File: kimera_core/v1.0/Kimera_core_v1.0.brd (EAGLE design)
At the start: 26 x 12 mm, 15 parts, among them IC1 PCA9555RGER, IC2 PCA9555RGER, Q1 CSTCR6M00G53Z, U1 ATMEGA32U4QFN

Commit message: kimera_core: Change bus and layout
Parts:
- added JP1, JP2, JP3, JP4: (no value), castellation:P12
- moved IC2 18.1 mm to (4.50, 10.5)
- moved C5 10.9 mm to (9.25, 10.0), turned to 90 degrees
- moved C1 4.47 mm to (13.4, 12.0)
- moved C2 4.47 mm to (11.0, 12.0)
- moved C3 4.47 mm to (12.2, 12.0)
- moved Q1 4.47 mm to (21.6, 3.80)
- moved R1 4.47 mm to (13.4, 4.00)
- moved R2 4.47 mm to (12.2, 4.00)
- moved R3 4.47 mm to (11.0, 4.00)
- moved R4 4.47 mm to (23.0, 12.0)
- moved R5 4.47 mm to (21.8, 12.0)
- moved R6 4.47 mm to (20.6, 12.0)
- moved U1 4.47 mm to (17.0, 8.00)
- moved C4 2.73 mm to (9.25, 5.00), turned to 270 degrees
- moved IC1 1.58 mm to (4.50, 4.50)
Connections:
- net N$1 renamed RESET
- net N$11 renamed SDA
- removed net N$10: IC1.19, R5.1, U1.18
- new net A1: IC1.23, IC2.23
- new net A2: IC1.24, IC2.24
- new net MISO: U1.11
- new net MOSI: U1.10
- new net P1: IC1.1, JP2.7
- new net P10: IC1.11, JP1.4
- new net P11: IC1.12, JP1.5
- new net P12: IC1.13, JP1.6
- new net P13: IC1.14, JP1.7
- new net P14: IC1.15, JP1.8
- new net P15: IC1.16, JP1.9
- new net P16: IC1.17, JP1.10
- new net P17: IC2.1, JP3.3
- new net P18: IC2.2, JP3.4
- new net P19: IC2.3, JP3.5
- new net P2: IC1.2, JP2.8
- new net P20: IC2.4, JP3.6
- new net P21: IC2.5, JP3.7
- new net P22: IC2.6, JP3.8
- new net P23: IC2.7, JP3.9
- new net P24: IC2.8, JP3.10
- new net P25: IC2.10, JP3.11
- new net P26: IC2.11, JP3.12
- new net P27: IC2.12, JP2.1
- new net P28: IC2.13, JP2.2
- new net P29: IC2.14, JP2.3
- new net P3: IC1.3, JP2.9
- new net P30: IC2.15, JP2.4
- new net P31: IC2.16, JP2.5
- new net P32: IC2.17, JP2.6
- new net P4: IC1.4, JP2.10
- new net P5: IC1.5, JP2.11
- new net P6: IC1.6, JP2.12
- new net P7: IC1.7, JP1.1
- new net P8: IC1.8, JP1.2
- new net P9: IC1.10, JP1.3
- new net RX: U1.20
- new net SCK: U1.9
- new net SCL: IC1.19, IC2.19, R5.1, U1.18
- new net TX: U1.21
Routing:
- net P17: track 0.00 -> 9.95 mm, vias 0 -> 1
- net P16: track 0.00 -> 9.45 mm, vias 0 -> 1
- net P18: track 0.00 -> 8.39 mm, vias 0 -> 1
- net P15: track 0.00 -> 7.89 mm, vias 0 -> 1
- net P19: track 0.00 -> 6.83 mm, vias 0 -> 1
- net P14: track 0.00 -> 6.33 mm, vias 0 -> 1
- net P20: track 0.00 -> 5.33 mm
- net P21: track 0.00 -> 4.68 mm
- net P13: track 0.00 -> 4.68 mm
- net GND: track 0.00 -> 4.15 mm
- net P26: track 0.00 -> 3.53 mm
- net P32: track 0.00 -> 3.53 mm
- net P27: track 0.00 -> 3.47 mm
- net P12: track 0.00 -> 3.47 mm
- net P22: track 0.00 -> 3.45 mm
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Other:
- board size 26 x 12 mm -> 25 x 15 mm

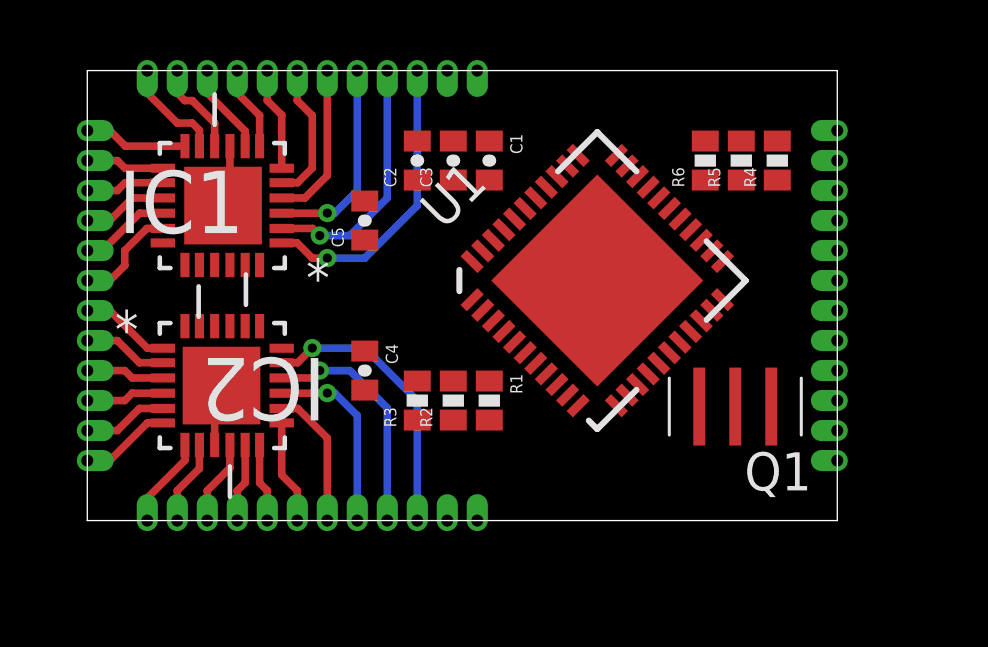
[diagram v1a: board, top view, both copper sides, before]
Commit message: kimera_core: Change basic layout and route a part of io
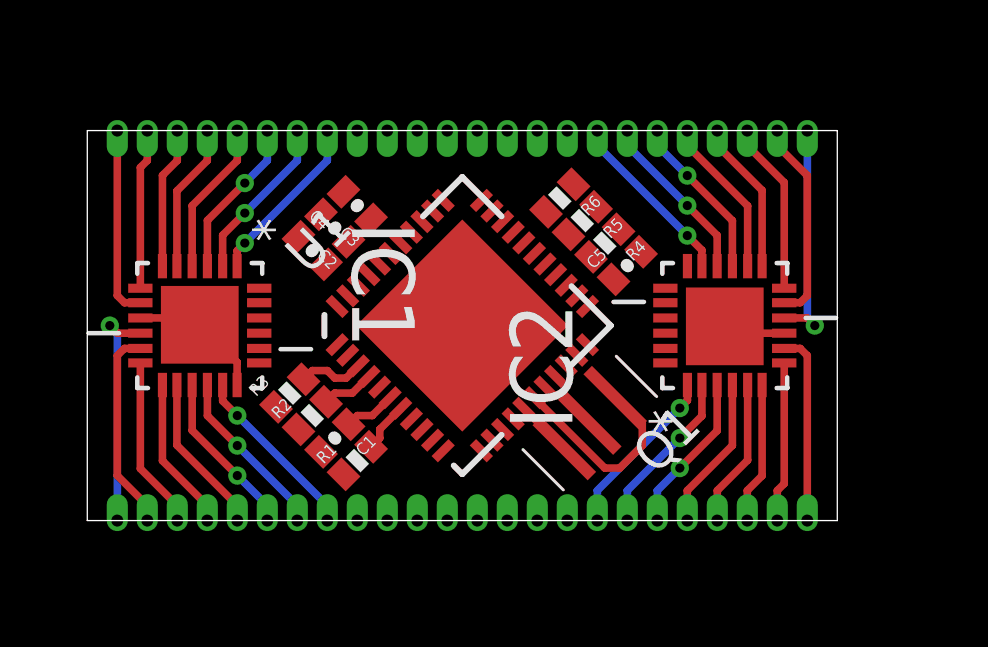
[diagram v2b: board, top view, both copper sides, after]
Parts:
- added JP5, JP6: (no value), castellation:P08
- JP1, JP2, JP3, JP4: device castellation:P12 -> castellation:P08
- moved IC2 17.2 mm to (21.2, 6.50), turned to 90 degrees
- moved JP3 15.5 mm to (17.0, 0.00), turned to 0 degrees
- moved JP1 14.3 mm to (8.00, 13.0), turned to 180 degrees
- moved JP2 13.0 mm to (1.00, 0.00), turned to 0 degrees
- moved JP4 11.0 mm to (24.0, 13.0), turned to 180 degrees
- moved C1 10.6 mm to (8.25, 2.75), turned to 225 degrees
- moved C5 8.88 mm to (18.0, 8.50), turned to 45 degrees
- moved R4 6.37 mm to (17.2, 9.25), turned to 225 degrees
- moved R5 5.66 mm to (16.5, 10.0), turned to 225 degrees
- moved R6 5.01 mm to (15.8, 10.8), turned to 225 degrees
- moved Q1 4.88 mm to (16.8, 3.25), turned to 225 degrees
- moved R1 4.83 mm to (9.00, 2.00), turned to 45 degrees
- moved U1 4.74 mm to (12.5, 6.50)
- moved R2 4.73 mm to (7.50, 3.50), turned to 45 degrees
- moved C4 4.37 mm to (7.50, 9.00), turned to 315 degrees
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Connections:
- net P1: now also JP1.1; no longer JP2.7
- net P10: now also JP2.2; no longer JP1.4
- net P11: now also JP2.3; no longer JP1.5
- net P12: now also JP2.4; no longer JP1.6
- net P13: now also JP2.5; no longer JP1.7
- net P14: now also JP2.6; no longer JP1.8
- net P15: now also JP2.7; no longer JP1.9
- net P16: now also JP2.8; no longer JP1.10
- net P17: now also JP3.1; no longer JP3.3
- net P18: now also JP3.2; no longer JP3.4
- net P19: now also JP3.3; no longer JP3.5
- net P2: now also JP1.2; no longer JP2.8
- net P20: now also JP3.4; no longer JP3.6
- net P21: now also JP3.5; no longer JP3.7
- net P22: now also JP3.6; no longer JP3.8
- net P23: now also JP3.7; no longer JP3.9
- net P24: now also JP3.8; no longer JP3.10
- net P25: now also JP4.1; no longer JP3.11
- net P26: now also JP4.2; no longer JP3.12
- net P27: now also JP4.3; no longer JP2.1
- net P28: now also JP4.4; no longer JP2.2
- net P29: now also JP4.5; no longer JP2.3
- net P3: now also JP1.3; no longer JP2.9
- net P30: now also JP4.6; no longer JP2.4
- net P31: now also JP4.7; no longer JP2.5
- net P32: now also JP4.8; no longer JP2.6
- net P4: now also JP1.4; no longer JP2.10
- net P5: now also JP1.5; no longer JP2.11
- net P6: now also JP1.6; no longer JP2.12
- net P7: now also JP1.7; no longer JP1.1
- net P8: now also JP1.8; no longer JP1.2
- net P9: now also JP2.1; no longer JP1.3
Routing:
- net N$3: track 0.00 -> 6.88 mm
- net P9: track 2.83 -> 7.73 mm, vias 0 -> 1
- net P25: track 3.18 -> 7.73 mm, vias 0 -> 1
- net P17: track 9.95 -> 5.76 mm
- net P10: track 2.63 -> 6.78 mm
- net P8: track 2.82 -> 6.37 mm
- net P16: track 9.45 -> 5.96 mm
- net P24: track 3.04 -> 6.37 mm
- net P26: track 3.53 -> 6.78 mm
- net P11: track 2.62 -> 5.77 mm
- net P18: track 8.39 -> 5.55 mm
- net P30: track 2.83 -> 5.56 mm, vias 0 -> 1
- net P3: track 2.62 -> 5.35 mm, vias 0 -> 1
- net P1: track 3.04 -> 5.76 mm, vias 0 -> 1
- net P29: track 2.63 -> 5.35 mm
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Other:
- board size 25 x 15 mm -> 25 x 13 mm

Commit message: kimera_core: Assign main io and route more io
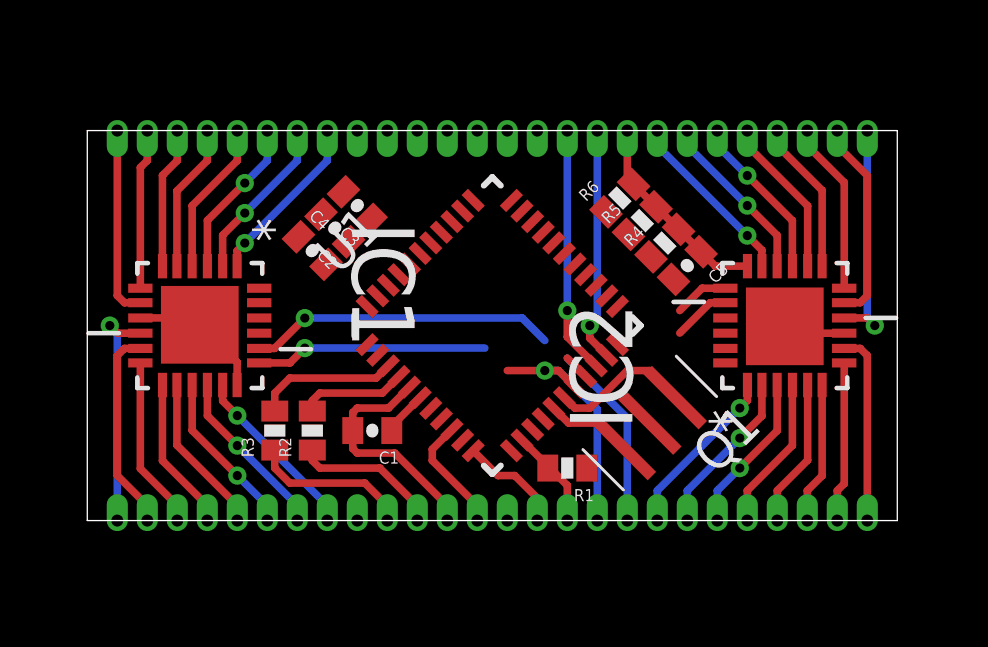
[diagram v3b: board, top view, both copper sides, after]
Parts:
- JP5, JP6: device castellation:P08 -> castellation:P10
- U1: value ATMEGA32U4QFN -> ATMEGA32U4QFN2; device SparkFun-DigitalIC:QFN-44 -> SparkFun-DigitalIC:QFN-44-NOPAD
- moved JP6 15.8 mm to (18.0, 13.0), turned to 180 degrees
- moved JP5 14.8 mm to (9.00, 0.00), turned to 0 degrees
- moved R1 7.00 mm to (16.0, 1.75), turned to 180 degrees
- moved C5 2.00 mm to (20.0, 8.50), turned to 225 degrees
- moved IC2 2.00 mm to (23.2, 6.50)
- moved JP3 2.00 mm to (19.0, 0.00)
- moved JP4 2.00 mm to (26.0, 13.0)
- moved Q1 2.00 mm to (18.8, 3.25)
- moved R4 2.00 mm to (19.2, 9.25), turned to 45 degrees
- moved R5 2.00 mm to (18.5, 10.0), turned to 45 degrees
- moved R6 2.00 mm to (17.8, 10.8), turned to 45 degrees
- moved R3 1.35 mm to (6.25, 3.00), turned to 90 degrees
- moved C1 1.27 mm to (9.50, 3.00), turned to 180 degrees
- moved U1 1.00 mm to (13.5, 6.50)
- moved R2 0.50 mm to (7.50, 3.00), turned to 90 degrees
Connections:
- removed net N$8: R2.1
- removed net N$9: R3.1
- new net D+: JP5.3, R2.1
- new net D-: JP5.2, R3.1
- new net N$10: JP6.4
- new net N$11: JP6.5
- new net N$13: JP6.6
- new net N$14: JP6.7
- new net N$15: JP6.8
- new net N$16: JP6.9
- new net N$17: JP6.10
- net 5V: now also JP5.1, JP6.1
- net GND: now also JP5.4
- net MISO: now also JP5.7
- net MOSI: now also JP5.6
- net RESET: now also JP5.8
- net RX: now also JP6.3
- net SCK: now also JP5.5
- net SCL: now also JP5.9
- net SDA: now also JP5.10
- net TX: now also JP6.2
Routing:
- net SDA: track 0.00 -> 19.3 mm, vias 0 -> 1
- net SCL: track 0.00 -> 18.0 mm, vias 0 -> 2
- net RX: track 0.00 -> 8.24 mm, vias 0 -> 1
- net TX: track 0.00 -> 7.83 mm, vias 0 -> 1
- net GND: track 6.67 -> 14.2 mm
- net D-: track 0.00 -> 5.37 mm
- net 5V: track 1.69 -> 6.80 mm
- net D+: track 0.00 -> 4.97 mm
- net SCK: track 0.00 -> 3.93 mm
- net MISO: track 0.00 -> 3.54 mm
- net RESET: track 0.00 -> 3.31 mm
- net N$5: track 2.22 -> 4.76 mm
- net N$3: track 6.88 -> 4.81 mm
- net N$2: track 1.78 -> 3.57 mm
- net N$4: track 1.91 -> 2.92 mm
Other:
- board size 25 x 13 mm -> 27 x 13 mm

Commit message: kimera_core: Change element location and castellated holes
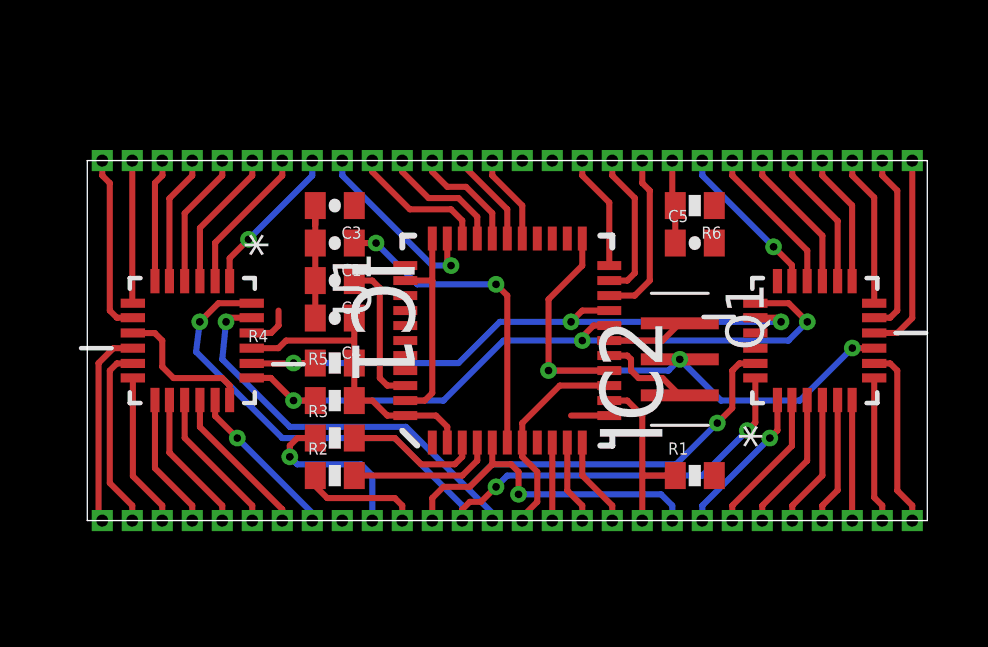
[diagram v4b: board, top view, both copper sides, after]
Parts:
- IC1, IC2: value PCA9555RGER -> PCA9555RGER-NOPAD; device Texas Instruments_By_element14_Batch_1:QFN50P400X400X100-25N -> pca9555:QFN50P400X400X100-25N-NOPAD
- JP5, JP6: device castellation:P10 -> castellation:P12
- moved R5 11.9 mm to (8.25, 4.00), turned to 0 degrees
- moved R4 11.7 mm to (8.25, 5.25), turned to 0 degrees
- moved C1 6.37 mm to (8.25, 9.25)
- moved R1 4.26 mm to (20.2, 1.50), turned to 0 degrees
- moved R6 2.51 mm to (20.2, 10.5), turned to 180 degrees
- moved C4 2.37 mm to (8.25, 6.75), turned to 180 degrees
- moved Q1 2.35 mm to (19.8, 5.38), turned to 270 degrees
- moved R3 2.02 mm to (8.25, 2.75), turned to 0 degrees
- moved JP4 1.80 mm to (27.5, 12.0)
- moved JP6 1.80 mm to (19.5, 12.0)
- moved C2 1.75 mm to (8.25, 8.00), turned to 180 degrees
- moved R2 1.68 mm to (8.25, 1.50), turned to 0 degrees
- moved JP3 1.50 mm to (20.5, 0.00)
- moved IC2 1.12 mm to (24.2, 6.00)
- moved JP1 1.12 mm to (7.50, 12.0)
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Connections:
- removed net 5V: C3.1, C4.1, C5.1, IC1.21, IC2.18, IC2.21, JP5.1, JP6.1, R1.2, R4.2, R5.2, R6.2, U1.14, U1.2, U1.24, U1.34, U1.44, U1.7
- removed net N$10: JP6.4
- removed net N$11: JP6.5
- removed net N$13: JP6.6
- removed net N$14: JP6.7
- removed net N$15: JP6.8
- removed net N$16: JP6.9
- removed net N$17: JP6.10
- new net /CTS: JP6.4, U1.22
- new net /RTS: JP6.5, U1.12
- new net L1: JP6.7, U1.27
- new net L2: JP6.8, U1.28
- new net L3: JP6.9, U1.29
- new net L4: JP6.10, U1.30
- new net L5: JP6.11, U1.31
- new net L6: JP6.12, U1.32
- new net VCC: C3.1, C4.1, C5.1, IC1.21, IC2.18, IC2.21, JP5.1, JP5.7, JP6.1, R1.2, R4.2, R5.2, R6.2, U1.14, U1.2, U1.24, U1.34, U1.44, U1.7
- net A1: now also JP5.6
- net A2: now also JP5.5
- net GND: now also JP5.12, JP6.6; no longer IC1.25, IC2.25
- net MISO: now also JP5.10; no longer JP5.7
- net MOSI: now also JP5.9; no longer JP5.6
- net RESET: now also JP5.11; no longer JP5.8
- net RX: now also JP6.2; no longer JP6.3
- net SCK: now also JP5.8; no longer JP5.5
- net SCL: no longer JP5.9
- net SDA: no longer JP5.10
- net TX: now also JP6.3; no longer JP6.2
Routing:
- net GND: track 14.2 -> 47.1 mm, vias 0 -> 4
- net A2: track 0.00 -> 27.3 mm, vias 0 -> 3
- net A1: track 0.00 -> 25.5 mm, vias 0 -> 2
- net VCC: track 0.00 -> 20.1 mm
- net N$6: track 1.49 -> 10.7 mm, vias 0 -> 2
- net 5V: track 6.80 -> 0.00 mm
- net L6: track 0.00 -> 6.32 mm, vias 0 -> 1
- net SCL: track 18.0 -> 23.8 mm, vias 2 -> 3
- net N$7: track 0.00 -> 4.91 mm
- net L5: track 0.00 -> 4.65 mm
- net L4: track 0.00 -> 4.22 mm
- net /CTS: track 0.00 -> 3.87 mm
- net L3: track 0.00 -> 3.79 mm
- net L2: track 0.00 -> 3.22 mm
- net L1: track 0.00 -> 3.01 mm
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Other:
- board size 27 x 13 mm -> 28 x 12 mm

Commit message: kimera_core: Reduce board size and remove some main io
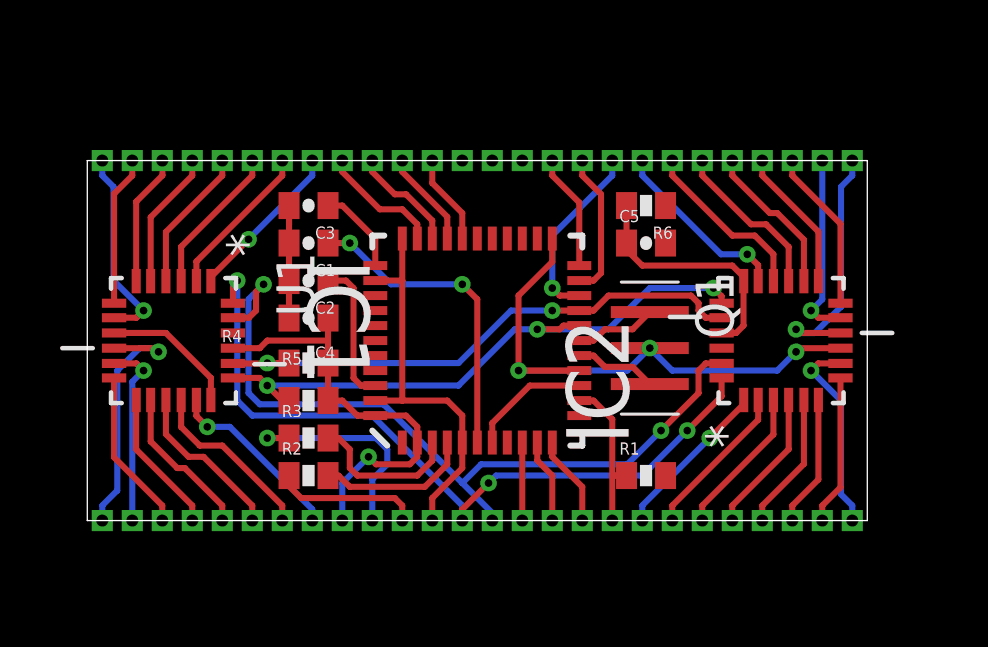
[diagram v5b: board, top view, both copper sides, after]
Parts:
- JP5, JP6: device castellation:P12 -> castellation:P10
- moved JP3 2.00 mm to (18.5, 0.00)
- moved JP4 2.00 mm to (25.5, 12.0)
- moved JP6 2.00 mm to (17.5, 12.0)
- moved C5 1.62 mm to (18.6, 9.25)
- moved R1 1.62 mm to (18.6, 1.50)
- moved R6 1.62 mm to (18.6, 10.5)
- moved IC2 1.12 mm to (23.1, 6.00)
- moved Q1 1.07 mm to (18.8, 5.75)
- moved U1 1.00 mm to (13.0, 6.00)
- moved C1 0.88 mm to (7.38, 9.25)
- moved C2 0.88 mm to (7.38, 8.00)
- moved C3 0.88 mm to (7.38, 10.5)
- moved C4 0.88 mm to (7.38, 6.75)
- moved R2 0.88 mm to (7.38, 1.50)
- moved R3 0.88 mm to (7.38, 2.75)
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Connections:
- removed net L5: JP6.11, U1.31
- removed net L6: JP6.12, U1.32
- net /CTS: now also JP6.3; no longer JP6.4
- net /RTS: now also JP6.4; no longer JP6.5
- net GND: no longer JP5.12, JP6.6
- net L1: now also U1.29; no longer U1.27
- net L2: now also U1.30; no longer U1.28
- net L3: now also U1.31; no longer U1.29
- net L4: now also U1.32; no longer U1.30
- net MISO: now also JP5.9; no longer JP5.10
- net MOSI: now also JP5.8; no longer JP5.9
- net RESET: now also JP5.10; no longer JP5.11
- net RX: now also JP6.1; no longer JP6.2
- net SCK: now also JP5.7; no longer JP5.8
- net SCL: now also JP6.5
- net SDA: now also JP6.6
- net TX: now also JP6.2; no longer JP6.3
- net VCC: no longer JP5.7, JP6.1
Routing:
- net VCC: track 20.1 -> 29.9 mm, vias 0 -> 1
- net L6: track 6.32 -> 0.00 mm, vias 1 -> 0
- net GND: track 47.1 -> 40.9 mm, vias 4 -> 3
- net L5: track 4.65 -> 0.00 mm
- net SCL: track 23.8 -> 20.5 mm
- net SDA: track 21.3 -> 18.4 mm, vias 3 -> 2
- net A2: track 27.3 -> 25.5 mm
- net P9: track 6.65 -> 8.50 mm, vias 0 -> 1
- net P25: track 6.72 -> 8.48 mm, vias 0 -> 1
- net D-: track 5.84 -> 7.46 mm
- net N$12: track 1.50 -> 0.00 mm
- net /RTS: track 1.27 -> 0.27 mm
- net A1: track 25.5 -> 26.4 mm
- net P32: track 5.26 -> 6.13 mm
- net D+: track 4.02 -> 4.89 mm
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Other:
- board size 28 x 12 mm -> 26 x 12 mm
